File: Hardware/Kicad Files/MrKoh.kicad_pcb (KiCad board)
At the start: 2 copper layers, 29.1 x 53.4 mm, 47 parts, among them J1 USB_C_Receptacle_USB2.0, J2 header, Q1 MMBT3904, SW1 RESET, SW2 BOOT, U1 USBLC6-2SC6, U2 ESP32-C3-FH4, U3 AZ1117-3.3, Y1 32K (C32346), Y2 40Mhz (C252256)

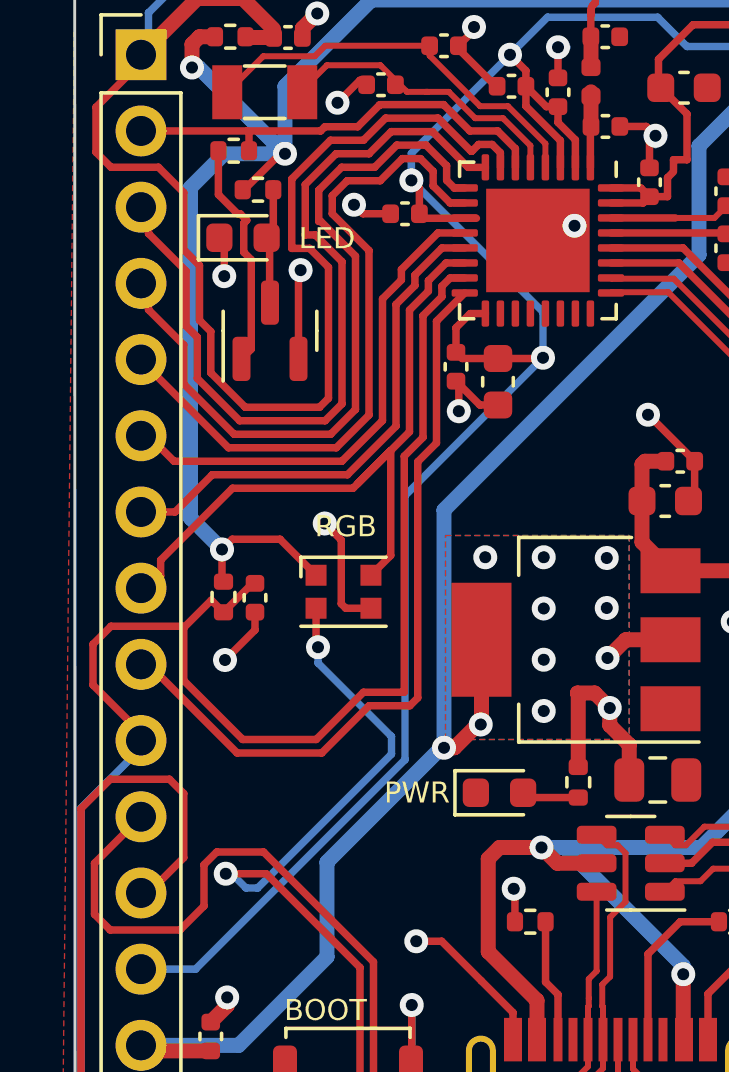
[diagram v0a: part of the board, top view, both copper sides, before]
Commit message: Part issue
There was a problem with sourcing the original RGB part and changes to schematic, pcb, and fabrication files.  Production proofs were added.
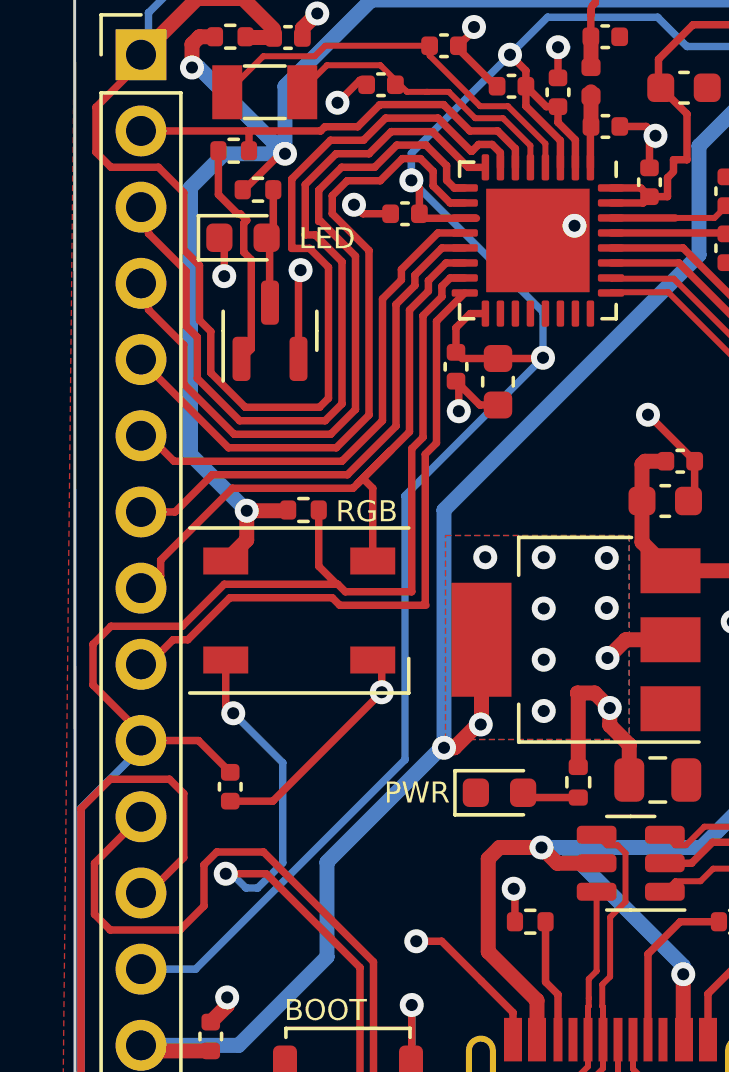
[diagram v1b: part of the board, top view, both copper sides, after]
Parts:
- D2: footprint LED_SMD:LED_WS2812B-2020_PLCC4_2.0x2.0mm -> LED_SMD:LED_WS2812B_PLCC4_5.0x5.0mm_P3.2mm
- moved C19 6.35 mm to (18.5, 59.9)
- moved R5 3.94 mm to (20.9, 50.7), turned to 0 degrees
- moved D2 1.60 mm to (20.8, 54.0)
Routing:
- net /GPIO10: track 25.1 -> 21.2 mm
- net /DOUT: track 31.3 -> 27.8 mm
- net /BOOT: track 72.9 -> 69.9 mm
- net +3V3: track 127.7 -> 125.3 mm
- net GND: track 49.0 -> 50.8 mm, vias 25 -> 24
- net /GPIO8: track 23.9 -> 22.4 mm
